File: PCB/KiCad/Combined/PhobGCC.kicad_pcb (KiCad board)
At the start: 2 copper layers, 143 x 91.4 mm, 75 parts, among them J1 Conn_01x06_Female, J2 Conn_01x04_Female, J3 Conn_01x01_Male, J4 Conn_01x04_Male, J5 Rumble, Q1 Q_NMOS_GSD, Q2 Q_PMOS_GDS, Q3 Q_NMOS_GSD, SW1 A, SW10 Dup, SW11 Dright, SW12 Ddown, SW2 B, SW3 X, SW4 Y, SW5 Start, SW6 L, SW7 R, SW8 Z, SW9 Dleft, U1 Teensy4.0, U2 2x DRV5053CAQLPGM Hall Effect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, U3 GP2S60-MFG, U4 GP2S60-MFG, U5 Stickbox_Assembly

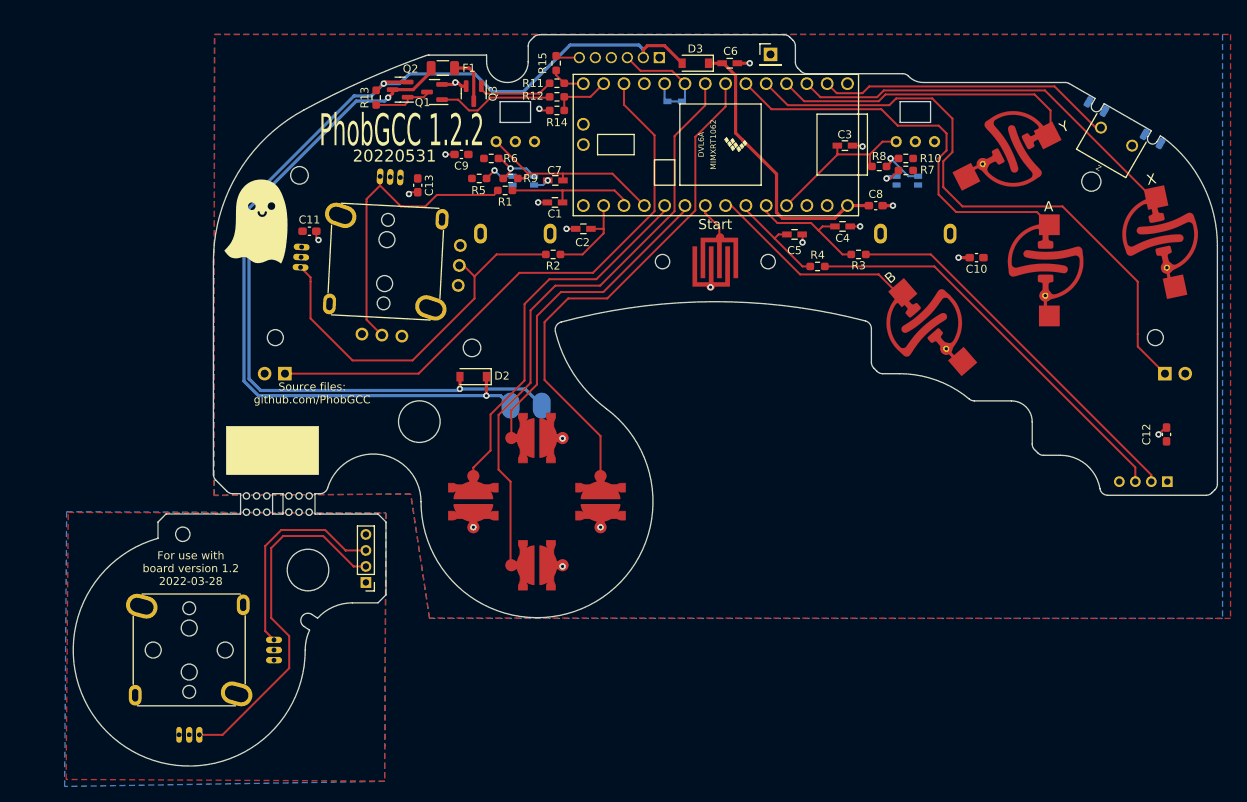
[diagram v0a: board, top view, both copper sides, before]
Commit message: Consolidated footprints to PhobGCC library
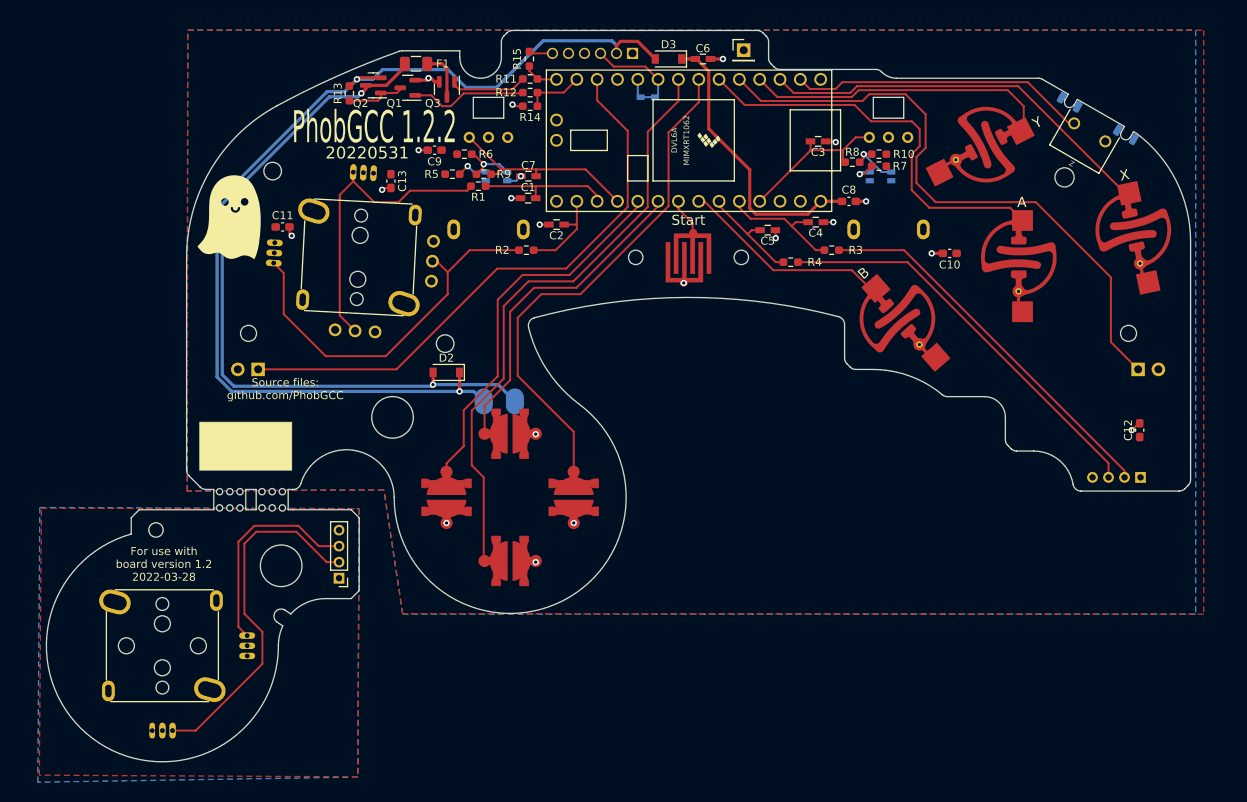
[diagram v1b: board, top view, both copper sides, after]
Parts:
- C1, C2, C3, C4, C5, C6, C7: footprint Capacitors_SMD:C_0603_HandSoldering -> PhobGCC_Footprints:C_0603_HandSoldering
- C10, C11, C12, C13, C8, C9: footprint Capacitor_SMD:C_0603_1608Metric_Pad1.08x0.95mm_HandSolder -> PhobGCC_Footprints:C_0603_1608Metric_Pad1.08x0.95mm_HandSolder
- D2, D3: footprint Diode_SMD:D_SOD-123 -> PhobGCC_Footprints:D_SOD-123
- F1: footprint Resistor_SMD:R_1206_3216Metric -> PhobGCC_Footprints:Fuse_1206_3216Metric
- J2: footprint Pin_Headers:Pin_Header_Straight_1x04_Pitch2.00mm -> PhobGCC_Footprints:PinHeader_1x04_P2.00mm_Vertical
- J3: footprint Connector_PinHeader_2.54mm:PinHeader_1x01_P2.54mm_Vertical -> PhobGCC_Footprints:PinHeader_1x01_P2.54mm_Vertical
- J4: footprint Connector_PinHeader_2.00mm:PinHeader_1x04_P2.00mm_Vertical -> PhobGCC_Footprints:PinHeader_1x04_P2.00mm_Vertical
- Q1, Q2, Q3: footprint Package_TO_SOT_SMD:SOT-23 -> PhobGCC_Footprints:SOT-23
- R1, R11, R12, R13, R14, R15, R2, R3, R4: footprint Resistor_SMD:R_0603_1608Metric_Pad0.98x0.95mm_HandSolder -> PhobGCC_Footprints:R_0603_1608Metric_Pad0.98x0.95mm_HandSolder
- R10, R5, R6, R7, R8, R9: footprint Resistor_SMD:R_0603_1608Metric_Pad0.98x0.95mm_HandSolder -> PhobGCC_Footprints:R_0603_1608_DNP
- moved C3 3.39 mm to (128.8, 39.4)
- moved SW7 3.39 mm to (168.8, 67.9)
- moved C11 3.39 mm to (61.8, 50.1)
- moved H11 3.39 mm to (61.6, 92.5)
- moved H14 3.39 mm to (55.4, 85.5)
- moved SW10 3.39 mm to (90.3, 76.0)
- moved C1 3.39 mm to (92.5, 46.5)
- moved C5 3.39 mm to (122.5, 50.5)
- moved C6 3.39 mm to (114.4, 29.1)
- moved C7 3.39 mm to (92.6, 43.8)
- moved C9 3.39 mm to (80.8, 40.5)
- moved D1 3.39 mm to (107.5, 33.9)
- moved D3 3.39 mm to (110.1, 29.1)
- moved G*** 3.39 mm to (55.4, 49.0)
- moved H5 3.39 mm to (106.0, 53.9)
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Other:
- outline, holes or cut-outs redrawn

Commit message: 1.2.3 changes
omron tactile z support, larger c stick pin holes, relocated C10 from underneath button pad
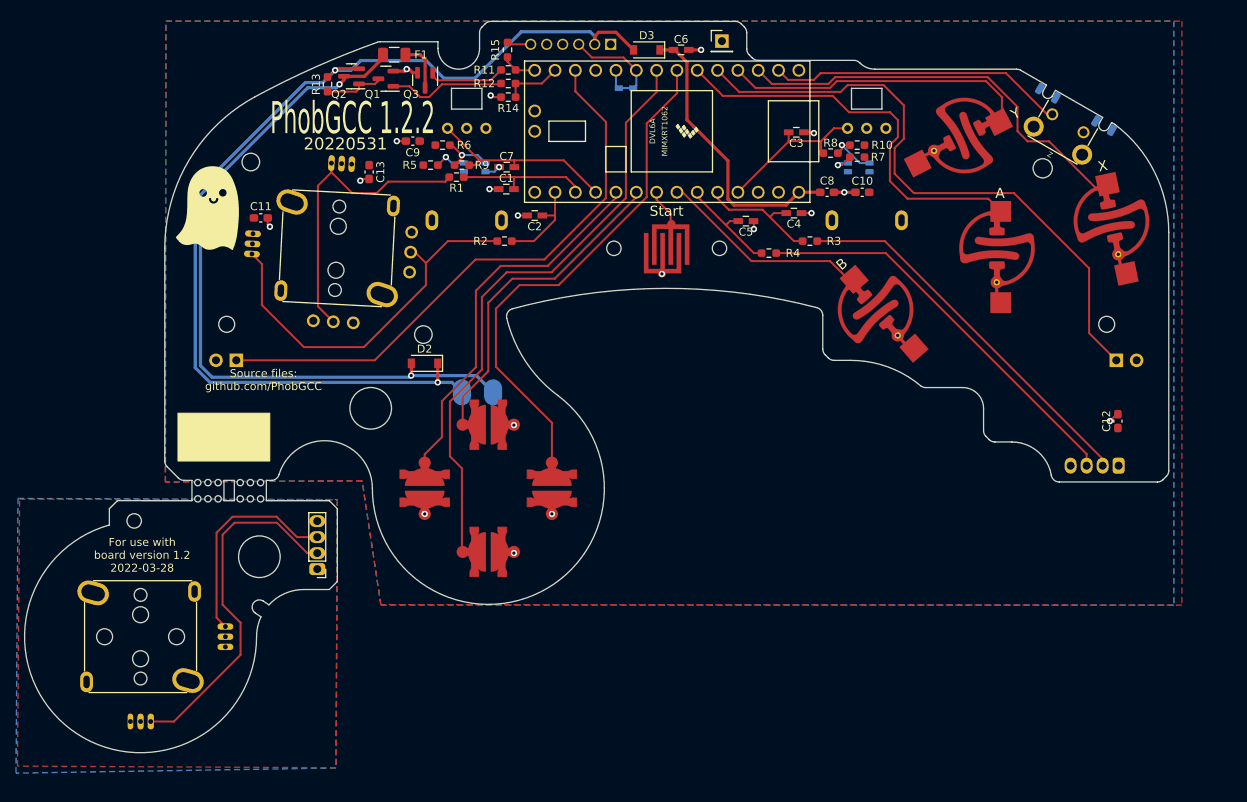
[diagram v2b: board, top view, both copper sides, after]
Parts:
- SW8: footprint PhobGCC_Footprints:Z_Switch_Edge -> PhobGCC_Footprints:Z_Switch_Edge_Omron
- moved C10 13.3 mm to (134.3, 45.8)
- moved J2 3.11 mm to (166.3, 80.0)
- moved C12 2.95 mm to (166.2, 74.4)
- moved SW12 2.95 mm to (87.5, 90.8)
- moved F1 2.95 mm to (75.8, 28.6)
- moved C1 2.95 mm to (89.8, 45.4)
- moved C2 2.95 mm to (93.3, 48.7)
- moved C4 2.95 mm to (125.7, 48.4)
- moved C7 2.95 mm to (89.8, 42.7)
- moved C8 2.95 mm to (129.9, 45.8)
- moved C9 2.95 mm to (78.1, 39.4)
- moved D1 2.95 mm to (104.7, 32.8)
- moved D3 2.95 mm to (107.3, 28.0)
- moved H4 2.95 mm to (164.8, 62.3)
- moved H7 2.95 mm to (156.8, 42.8)
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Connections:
- SW8 pad 3: unconnected-(SW8-Pad3) -> (no net)
- SW8 pad 4: unconnected-(SW8-Pad4) -> (no net)
- SW8 pad 5: unconnected-(SW8-Pad5) -> (no net)
- SW8 pad 6: unconnected-(SW8-Pad6) -> (no net)
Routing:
- net /X: track 50.2 -> 51.8 mm
- net GND: track 23.9 -> 24.0 mm, vias 20 -> 19
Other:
- outline, holes or cut-outs redrawn

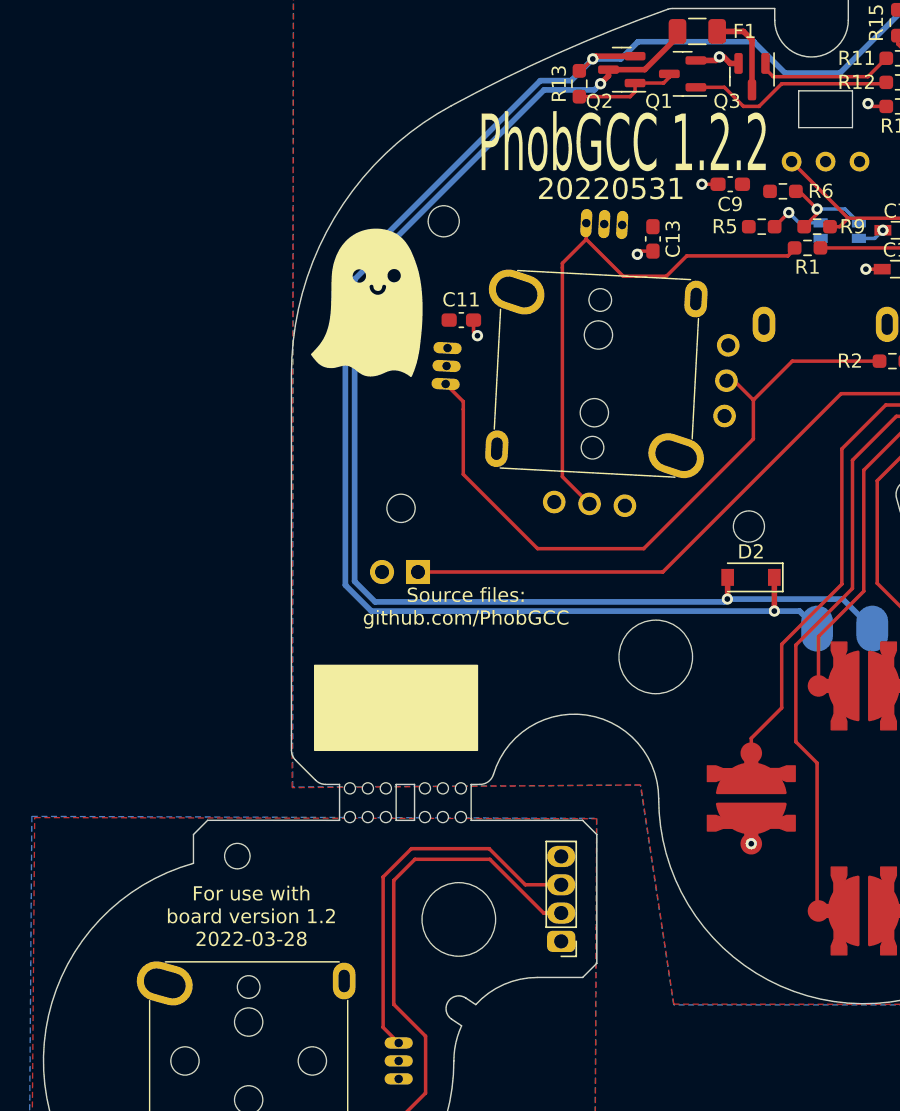
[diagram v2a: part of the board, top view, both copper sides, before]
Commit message: added back mini ghost
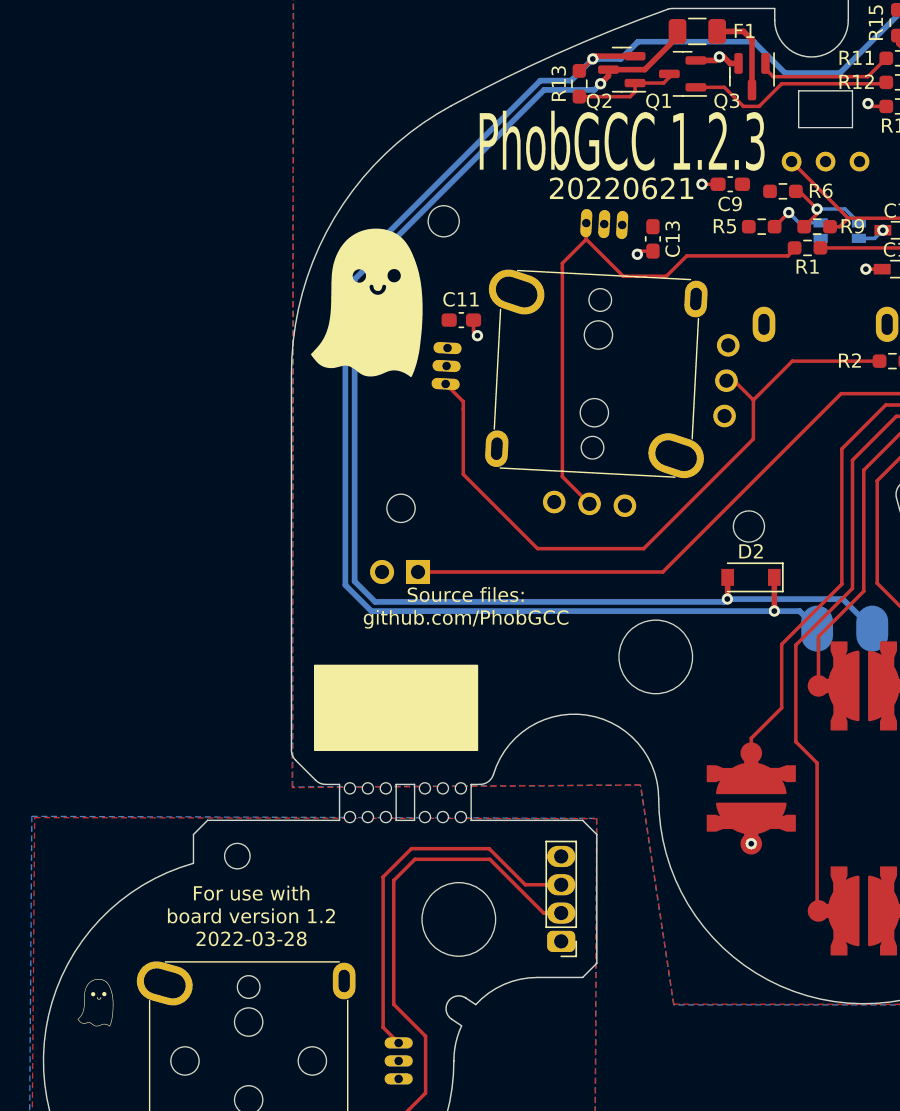
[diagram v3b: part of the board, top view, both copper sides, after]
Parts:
- added G***: LOGO, PhobGCC_Footprints:Ghost Logo Small, F.Cu at (33.3, 97.3)
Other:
- board text added: "20220621"
- board text added: "PhobGCC 1.2.3"
- board text removed: "20220531"
- board text removed: "PhobGCC 1.2.2"

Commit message: attempt at v1.2.4
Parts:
- removed D1: D_Schottky_Shorted, PhobGCC_Footprints:D_SOD-523_Shorted
- removed R10, R5, R6, R7, R8, R9: DNP, PhobGCC_Footprints:R_0603_1608_DNP
- removed U3, U4: GP2S60-MFG, PhobGCC_Footprints:Sharp_Microelectronics-GP2S60-MFG
- added TSTP1: testing pads, Library:testing pads, F.Cu at (70.6, 66.3)
- added TSTP2: testing pads, Library:testing pads, F.Cu at (85.3, 54.9)
- moved C11 15.2 mm to (68.1, 61.2), turned to 90 degrees
- moved C13 14.8 mm to (80.8, 55.7), turned to 180 degrees
- moved R1 12.4 mm to (92.4, 52.6)
- moved C1 9.48 mm to (98.0, 50.1), turned to 90 degrees
- moved C3 7.34 mm to (133.1, 36.3), turned to 90 degrees
- moved R2 3.04 mm to (92.5, 51.1)
- moved H4 3.00 mm to (167.8, 61.7)
- moved H7 3.00 mm to (159.8, 42.2)
- moved J2 3.00 mm to (169.2, 79.3)
- moved RV2 3.00 mm to (137.8, 37.2)
- moved SW1 3.00 mm to (154.0, 52.1)
- moved SW4 3.00 mm to (150.0, 38.0)
- moved SW8 3.00 mm to (162.9, 36.6)
- moved G*** 3.00 mm to (36.2, 96.7)
- moved H1 3.00 mm to (75.8, 72.2)
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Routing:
- net /Stick_y: track 47.6 -> 14.3 mm
- net /Stick_x: track 38.1 -> 27.7 mm
- net Net-(R6-Pad2): track 6.75 -> 0.00 mm, vias 1 -> 0
- net Net-(R10-Pad2): track 6.58 -> 0.00 mm, vias 1 -> 0
- net VCC: track 0.00 -> 4.44 mm, vias 0 -> 2
- net Net-(R5-Pad2): track 3.96 -> 0.00 mm, vias 1 -> 0
- net /Data: track 15.0 -> 11.1 mm
- net +3V3: track 0.00 -> 3.59 mm, vias 0 -> 2
- net Net-(R7-Pad2): track 3.28 -> 0.00 mm, vias 1 -> 0
- net /Stick_x_filt: track 16.7 -> 14.0 mm
- net /Ranalog: track 19.4 -> 17.0 mm
- net GND: track 24.0 -> 26.0 mm
- net /Stick_y_filt: track 11.7 -> 9.83 mm
- net /L: track 72.1 -> 73.7 mm
- net /Lanalog: track 24.2 -> 22.7 mm
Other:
- board text added: "20221007"
- board text added: "For use with board version 1.2.x 2022-10-07"
- board text added: "PhobGCC 1.2.4"
- board text removed: "20220621"
- board text removed: "For use with board version 1.2 2022-03-28"
- board text removed: "PhobGCC 1.2.3"

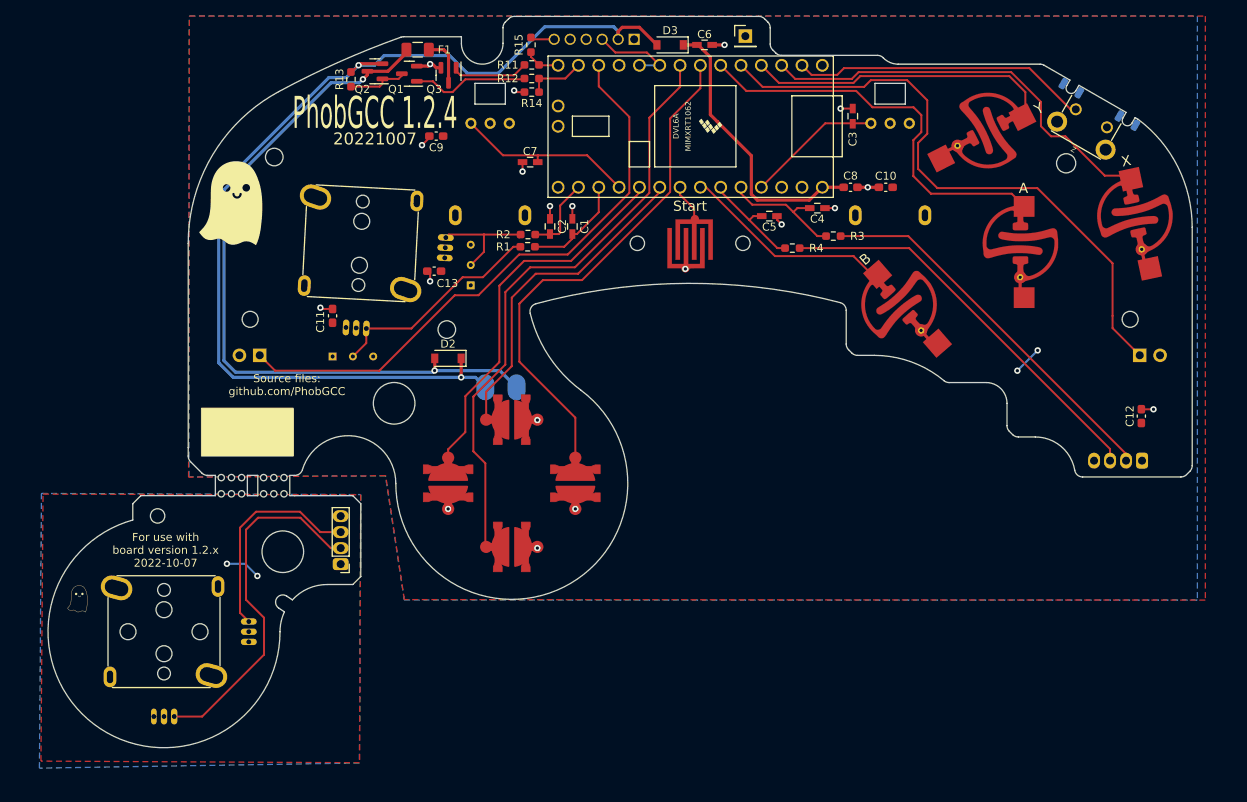
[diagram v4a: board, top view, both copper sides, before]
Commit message: elongate pads, flip wire mount cstick, z 1.1mm hole
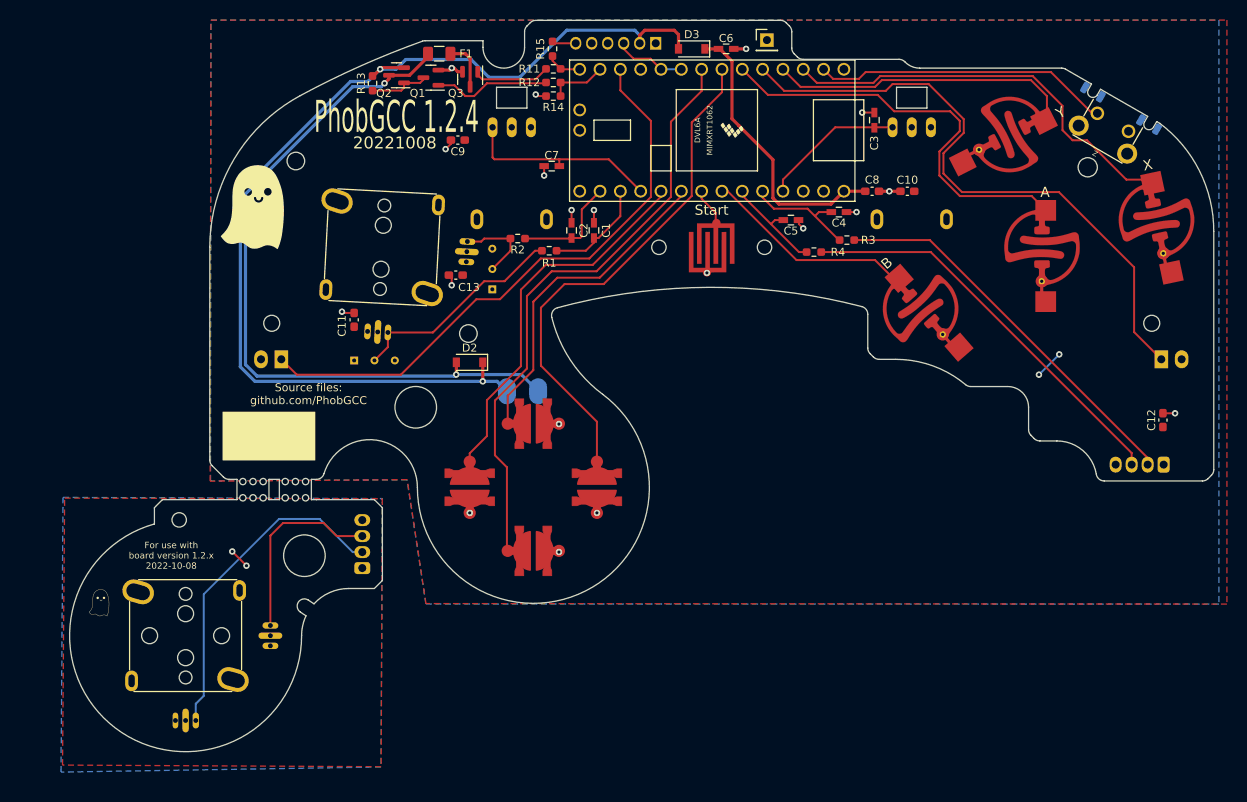
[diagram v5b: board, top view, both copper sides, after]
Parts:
- J4: moved to B.Cu
- moved C12 2.74 mm to (171.9, 74.3)
- moved H2 2.74 mm to (175.3, 77.7)
- moved SW2 2.74 mm to (141.5, 60.3)
- moved SW3 2.74 mm to (171.0, 49.2)
- moved C4 2.74 mm to (131.4, 48.3)
- moved C8 2.74 mm to (135.5, 45.7)
- moved C11 2.74 mm to (70.8, 61.7)
- moved C13 2.74 mm to (83.5, 56.2)
- moved D2 2.74 mm to (85.2, 67.1)
- moved G*** 2.74 mm to (38.9, 97.2)
- moved H1 2.74 mm to (78.5, 72.7)
- moved H10 2.74 mm to (48.9, 86.8)
- moved H11 2.74 mm to (64.5, 91.2)
- moved H12 2.74 mm to (45.2, 101.2)
- moved H13 2.74 mm to (54.2, 101.2)
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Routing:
- net VCC: track 4.44 -> 0.00 mm, vias 2 -> 0
- net /Stick_y: track 14.3 -> 10.3 mm
- net /Stick_y_filt: track 9.83 -> 13.8 mm
- net Net-(J4-Pad2): track 45.0 -> 41.6 mm
- net Net-(J4-Pad3): track 26.7 -> 24.0 mm
- net GND: track 26.0 -> 28.4 mm, vias 19 -> 21
- net /Lanalog: track 22.7 -> 24.9 mm
- net /Data: track 11.1 -> 9.26 mm
- net /A: track 50.4 -> 52.1 mm
- net +5V: track 131.4 -> 132.6 mm
- net /C_x_filt: track 16.0 -> 14.9 mm
- net /R: track 76.9 -> 77.9 mm
- net /C_x: track 47.9 -> 48.8 mm
- net /Ranalog: track 17.0 -> 17.9 mm
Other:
- board text added: "20221008"
- board text added: "For use with board version 1.2.x 2022-10-08"
- board text removed: "20221007"
- board text removed: "For use with board version 1.2.x 2022-10-07"
